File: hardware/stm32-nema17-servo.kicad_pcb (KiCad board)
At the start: 2 copper layers, 48 x 43.9 mm, 98 parts, among them J1 Conn_01x05, J2 C31-S-RA-CS1A-BK-SS, J3 TC-2050, J4 Screw_Terminal_01x02, J5 Screw_Terminal_01x02, J7 Conn_01x03, J8 Conn_01x03, J9 Conn_01x02, M1 Stepper_Motor_bipolar, Q1 NVTFS5C658NL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

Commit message: v0.3.1 board
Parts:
- M1: value Stepper_Motor_bipolar -> Motor_2_or_3_phase; footprint Connector_PinHeader_2.54mm:PinHeader_1x04_P2.54mm_Vertical -> Connector_PinHeader_2.54mm:PinHeader_1x06_P2.54mm_Vertical
- moved M1 2.62 mm to (143.7, 142.3)
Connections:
- M1 pad 2: OB -> OA
- M1 pad 4: OC -> OB
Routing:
- net GND: track 105.2 -> 137.8 mm, vias 57 -> 59
- net Net-(Q4-Pad4): track 19.5 -> 18.5 mm
- net RB: track 18.0 -> 17.2 mm
- net RA: track 11.1 -> 10.4 mm
- net VDD: track 106.7 -> 107.2 mm
- net Net-(Q5-Pad4): track 17.6 -> 17.1 mm
- net OA: track 14.3 -> 13.8 mm
- net Net-(Q3-Pad4): track 11.3 -> 10.8 mm
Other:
- board size 48 x 43.9 mm -> 48 x 44.5 mm
- board text added: "A-A-B-B-C-C"
- board text added: "STM32-NEMA17-SERVO V0.3.1 (c) 2020-04 dgulyas@inrobco.de"
- board text removed: "A-B-B-C"
- board text removed: "STM32-NEMA17-SERVO V0.3 (c) 2020-03 dgulyas@inrobco.de"

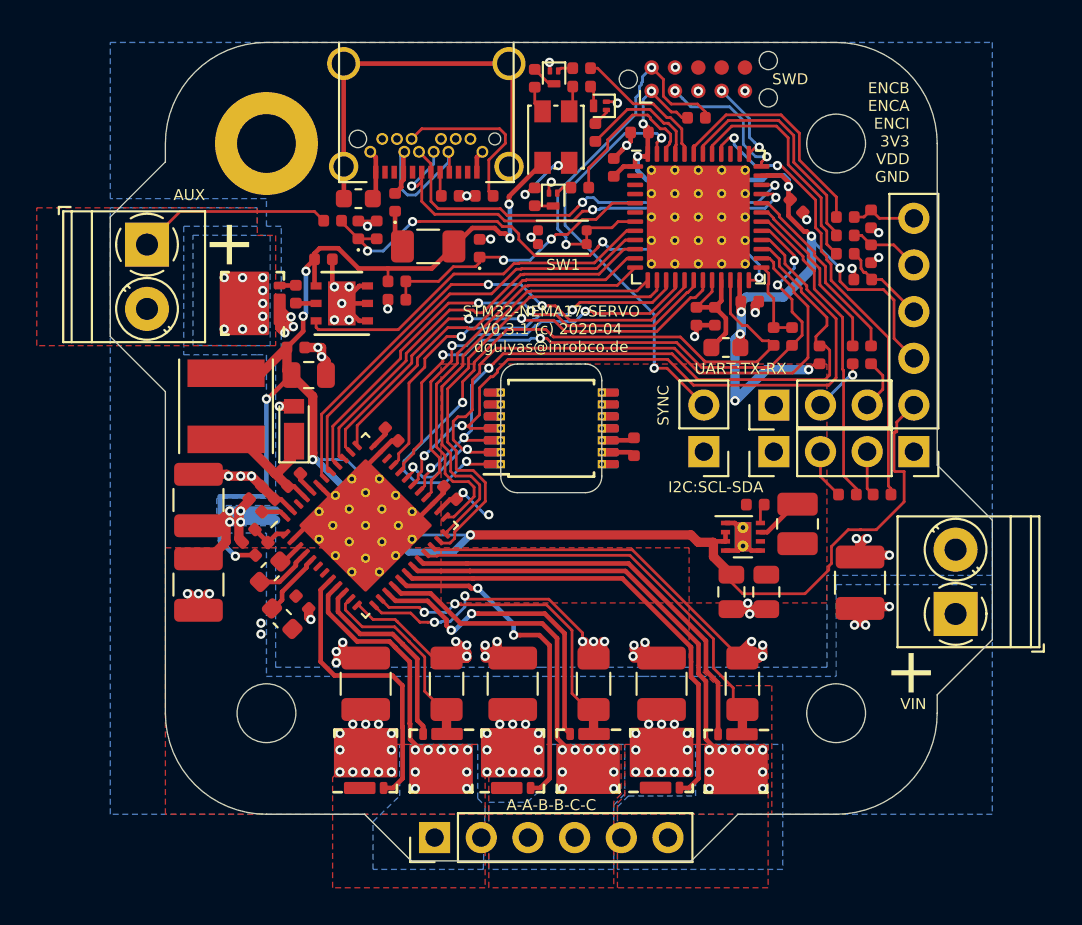
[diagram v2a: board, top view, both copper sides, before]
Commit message: 4 layer board design
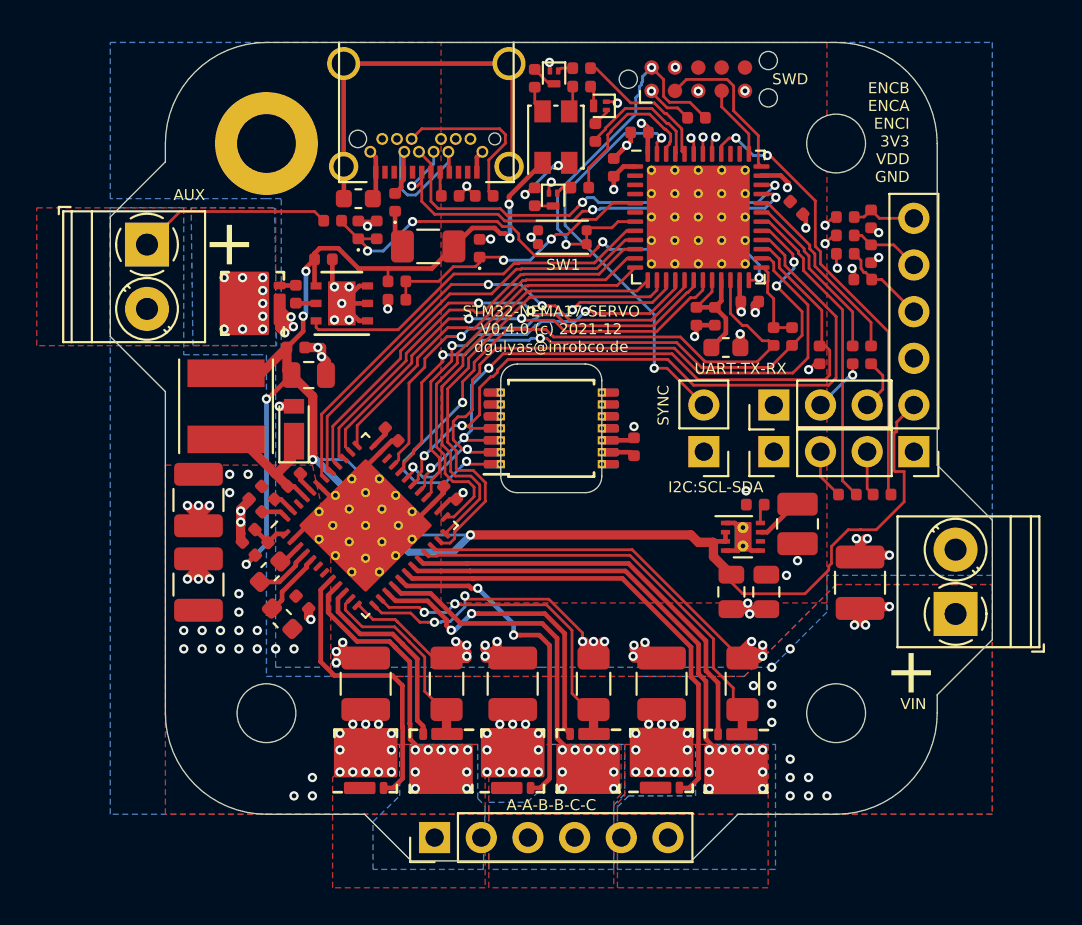
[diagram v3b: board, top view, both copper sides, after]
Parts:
- moved C3 0.10 mm to (163.3, 108.0)
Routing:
- net +3V3: track 58.7 -> 14.6 mm
- net VBUS: track 22.4 -> 15.0 mm, vias 47 -> 71
- net GND: track 137.8 -> 135.0 mm, vias 59 -> 63
- net VDD: track 107.2 -> 105.0 mm
- net ENCI: track 12.7 -> 14.1 mm, vias 0 -> 2
- net ENCA: track 12.7 -> 14.1 mm, vias 0 -> 2
- net ENCB: track 12.7 -> 11.6 mm, vias 0 -> 2
- net SWDIO: track 7.90 -> 8.61 mm, vias 2 -> 0
- net MISO: track 39.1 -> 38.4 mm
- net SWCLK: track 4.63 -> 4.04 mm, vias 2 -> 0
- added copper zone on In2.Cu, net +3V3
- added copper zone on In1.Cu, net GND
- added copper zone on In2.Cu, net GND
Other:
- copper layers 2 -> 4
- board text added: "STM32-NEMA17-SERVO V0.4.0 (c) 2021-12 dgulyas@inrobco.de"
- board text removed: "STM32-NEMA17-SERVO V0.3.1 (c) 2020-04 dgulyas@inrobco.de"

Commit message: cosmetic updates to some of the pcb footprints, mainly for better 3D models
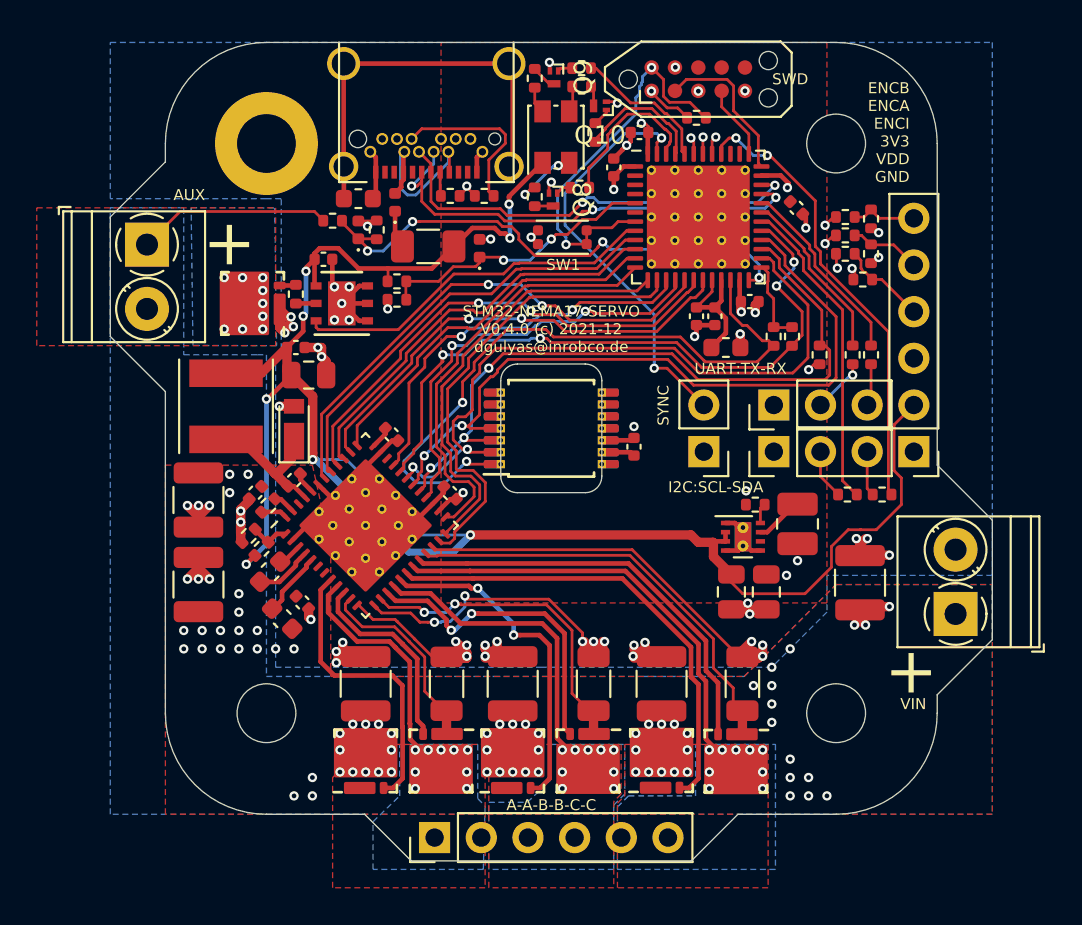
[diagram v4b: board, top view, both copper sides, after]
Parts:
- L4: footprint Inductor_SMD:L_Taiyo-Yuden_NR-50xx -> stm32-nema17:L_Taiyo-Yuden_NR-50xx
- Q10, Q8, Q9: footprint Package_TO_SOT_SMD:SOT-883 -> Package_DFN_QFN:Diodes_DFN1006-3
- U3: footprint Package_SON:Texas_PWSON-N6 -> stm32-nema17:Texas_PWSON-N6
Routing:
- net Net-(J7-Pad3): track 2.86 -> 2.33 mm
- net ENCI: track 14.1 -> 13.6 mm
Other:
- net class Default removed
- board text added: "12V-48V INPUT"
- board text added: "GND"
- board text removed: "GND 12V-48V INPUT"

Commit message: tweaks to v0.4.0 hardware design
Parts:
- J2: footprint stm32-nema17:USB_C_Receptacle_Adam_C31-S-RA-CS1A-BK-SS -> stm32-nema17:USB_C_Receptacle_Adam_C31-S-RA-CS1X-BK
- L4: footprint stm32-nema17:L_Taiyo-Yuden_NR-50xx -> Inductor_SMD:L_Taiyo-Yuden_NR-50xx
- Q10, Q8, Q9: footprint Package_DFN_QFN:Diodes_DFN1006-3 -> Package_TO_SOT_SMD:SOT-883
- U3: footprint stm32-nema17:Texas_PWSON-N6 -> Package_SON:Texas_PWSON-N6
- moved R18 0.50 mm to (149.6, 101.0)
- moved R5 0.45 mm to (146.4, 107.8)
- moved R4 0.45 mm to (144.5, 107.8)
- moved Q9 0.45 mm to (150.6, 100.9)
- moved R15 0.45 mm to (152.1, 100.4)
- moved R19 0.45 mm to (152.1, 101.4)
- moved L1 0.40 mm to (139.5, 107.9)
- moved D4 0.40 mm to (139.5, 109.6)
- moved R28 0.40 mm to (138.1, 109.1)
- moved R29 0.39 mm to (140.5, 109.6)
- moved D1 0.30 mm to (141.5, 108.0)
- moved J2 0.25 mm to (143.2, 98.8)
- moved C14 0.10 mm to (159.7, 128.9)
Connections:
- J2 pad A8: Net-(J2-PadA8) -> unconnected-(J2-PadA8)
- J2 pad B8: Net-(J2-PadB8) -> unconnected-(J2-PadB8)
- J3 pad 6: Net-(J3-Pad6) -> unconnected-(J3-Pad6)
- J3 pad 7: Net-(J3-Pad7) -> unconnected-(J3-Pad7)
- J3 pad 8: Net-(J3-Pad8) -> unconnected-(J3-Pad8)
- U1 pad 2: Net-(U1-Pad2) -> unconnected-(U1-Pad2)
- U1 pad 3: Net-(U1-Pad3) -> unconnected-(U1-Pad3)
- U1 pad 38: Net-(U1-Pad38) -> unconnected-(U1-Pad38)
- U1 pad 39: Net-(U1-Pad39) -> unconnected-(U1-Pad39)
- U1 pad 4: Net-(U1-Pad4) -> unconnected-(U1-Pad4)
- U1 pad 6: Net-(U1-Pad6) -> unconnected-(U1-Pad6)
- U4 pad 10: Net-(U4-Pad10) -> unconnected-(U4-Pad10)
- U4 pad 14: Net-(U4-Pad14) -> unconnected-(U4-Pad14)
- U4 pad 6: Net-(U4-Pad6) -> unconnected-(U4-Pad6)
- U4 pad 7: Net-(U4-Pad7) -> unconnected-(U4-Pad7)
- U4 pad 8: Net-(U4-Pad8) -> unconnected-(U4-Pad8)
- U4 pad 9: Net-(U4-Pad9) -> unconnected-(U4-Pad9)
- U6 pad 34: Net-(U6-Pad34) -> unconnected-(U6-Pad34)
- U6 pad 46: Net-(U6-Pad46) -> unconnected-(U6-Pad46)
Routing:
- net Net-(J2-PadB5): track 9.27 -> 12.0 mm, vias 0 -> 1
- net VDD: track 104.5 -> 106.0 mm
- net GND: track 135.0 -> 134.0 mm
- net Net-(D1-Pad2): track 9.73 -> 10.4 mm
- net Net-(J2-PadS1): track 22.1 -> 22.7 mm
- net DM: track 25.8 -> 26.4 mm
- net VBUS: track 15.0 -> 15.1 mm, vias 71 -> 69
